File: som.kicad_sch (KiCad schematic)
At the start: 14 parts

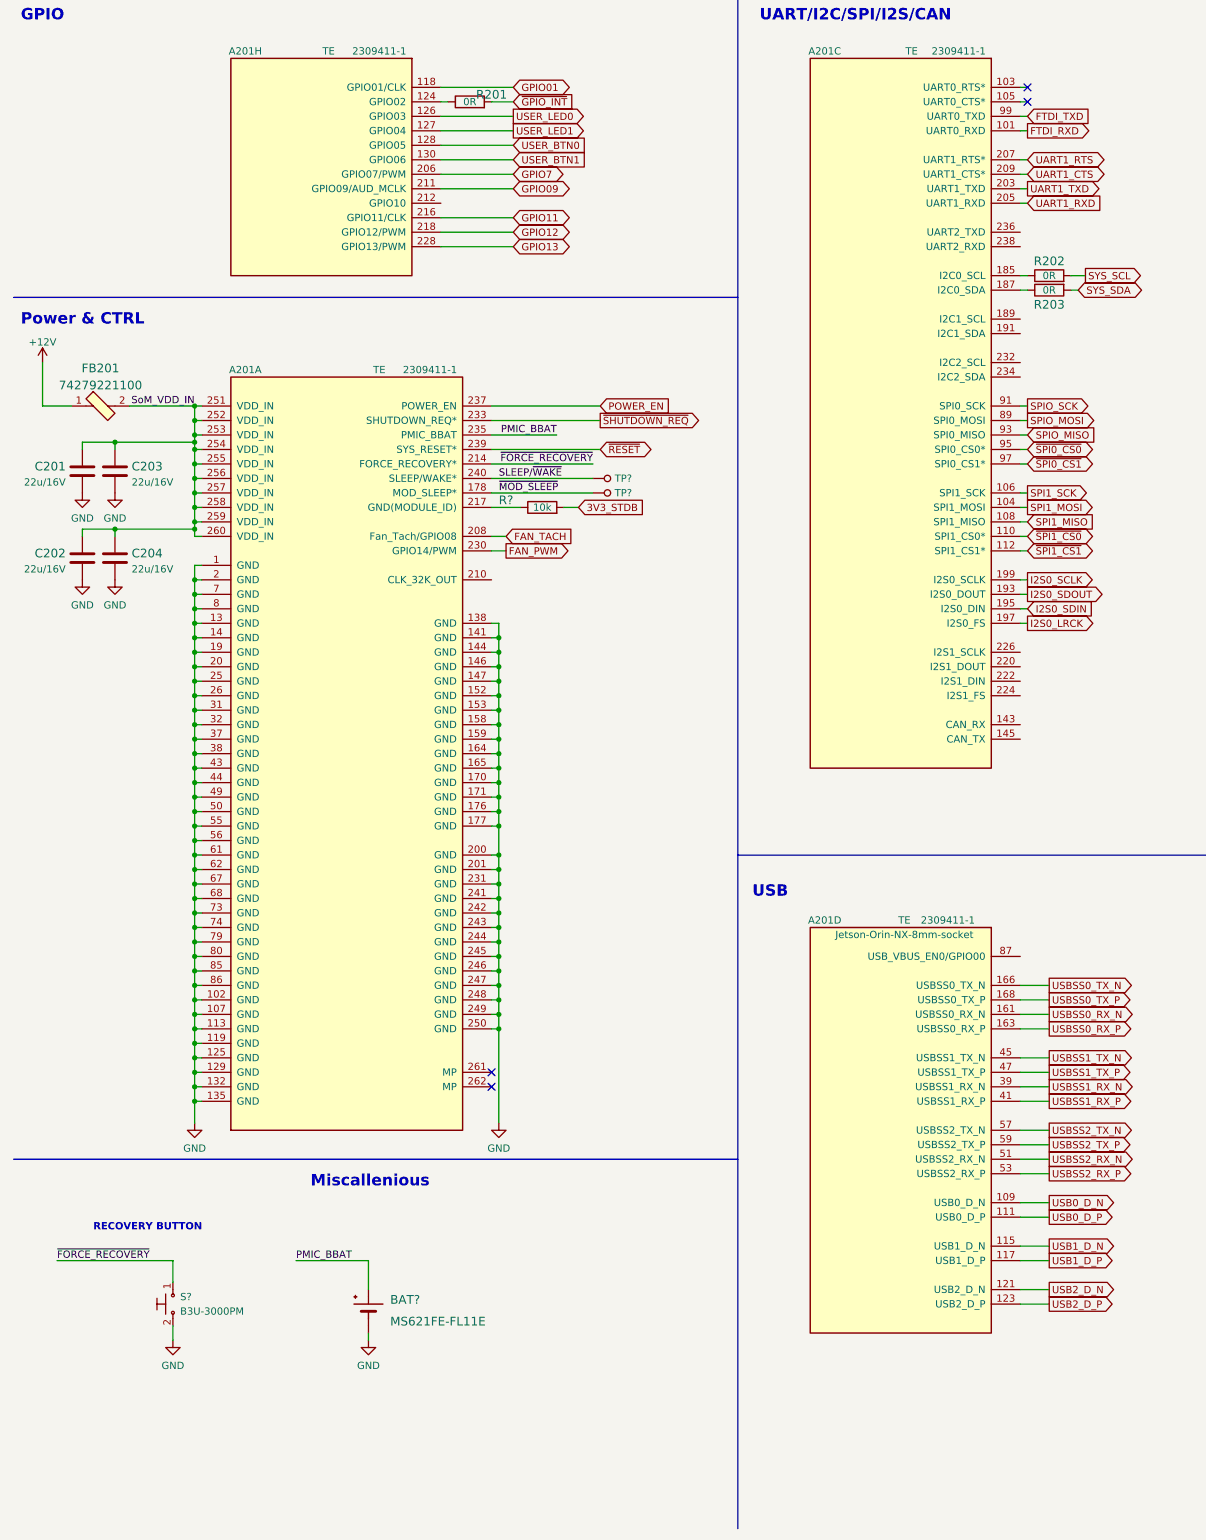
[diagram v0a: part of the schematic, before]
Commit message: Added buffer for debug UART
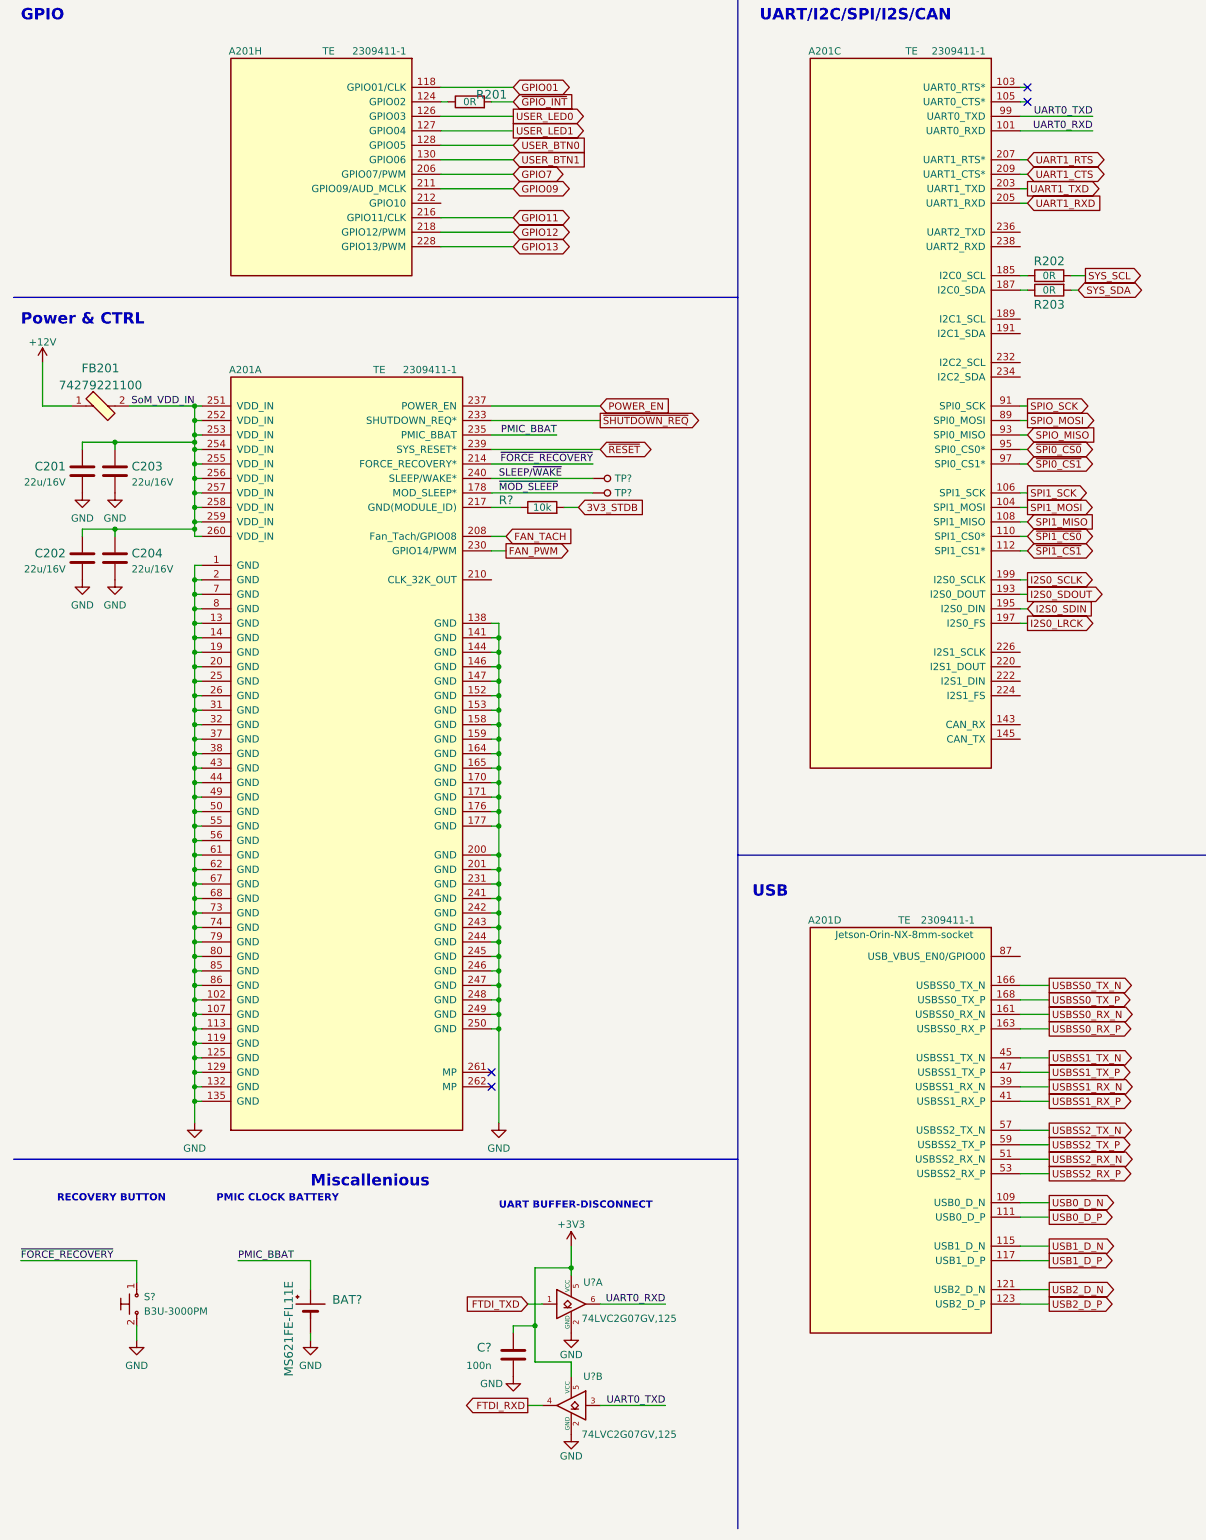
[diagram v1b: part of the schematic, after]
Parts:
- added C?: C_100n_0402, antmicro-footprints:0402-cap, symbol antmicroCapacitors0402:C_100n_0402
- added U? (x2): 74LVC2G07GV,125, antmicro-footprints:SC-74, symbol antmicroLogicBuffersDriversReceiversTransceivers:74LVC2G07GV,125
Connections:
- net FTDI_RXD: now also U?.4; no longer A201.101 (UART0_RXD)
- net FTDI_TXD: now also U?.1; no longer A201.99 (UART0_TXD)
- net GND: now also C?.2, U?.2 (GND), U?.2 (GND)
- new net +3V3: C?.1, U?.5 (VCC), U?.5 (VCC)
- new net UART0_RXD: A201.101 (UART0_RXD), U?.6
- new net UART0_TXD: A201.99 (UART0_TXD), U?.3
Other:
- note added: "PMIC CLOCK BATTERY"
- note added: "UART BUFFER-DISCONNECT"
- moved on the sheet: BAT?, S?

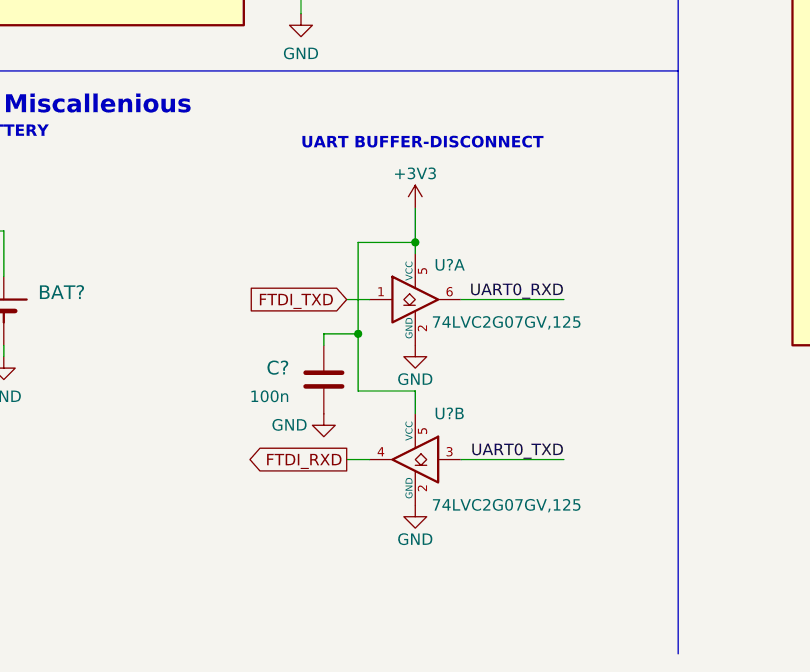
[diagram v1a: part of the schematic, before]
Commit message: Changed UART buffer for ones with push-pull output
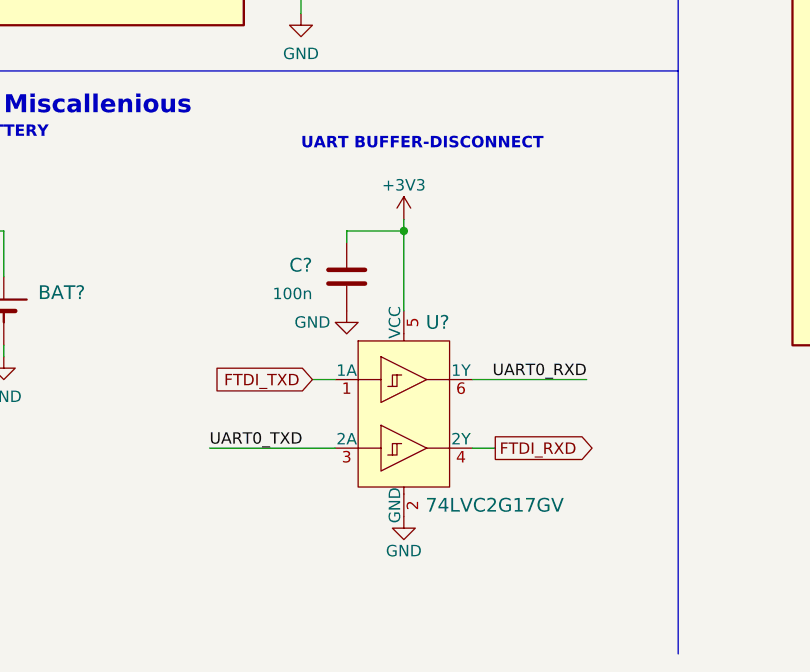
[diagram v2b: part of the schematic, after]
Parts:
- removed C?: C_100n_0402, antmicro-footprints:0402-cap, symbol antmicroCapacitors0402:C_100n_0402
- removed U? (x2): 74LVC2G07GV,125, antmicro-footprints:SC-74, symbol antmicroLogicBuffersDriversReceiversTransceivers:74LVC2G07GV,125
- added C?: C_100n_0402, antmicro-footprints:0402-cap, symbol antmicroCapacitors0402:C_100n_0402
- added U?: 74LVC2G17GV, antmicro-footprints:SC-74, symbol antmicroLogicBuffersDriversReceiversTransceivers:74LVC2G17GV
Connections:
- net +3V3: now also C?.1, U?.5 (VCC)
- net FTDI_RXD: now also U?.4 (2Y)
- net FTDI_TXD: now also U?.1 (1A)
- net GND: now also C?.2, U?.2 (GND)
- net UART0_RXD: now also U?.6 (1Y)
- net UART0_TXD: now also U?.3 (2A)

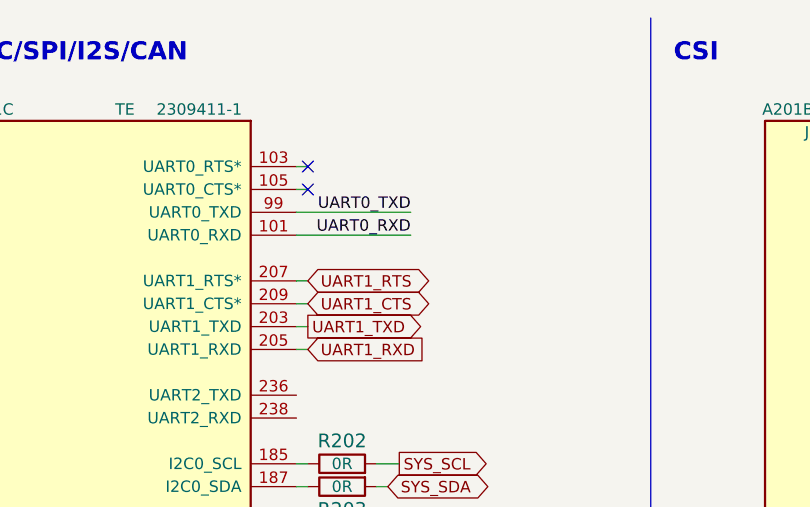
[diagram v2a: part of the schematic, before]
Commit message: Added 0Ohm resistors for debug UART
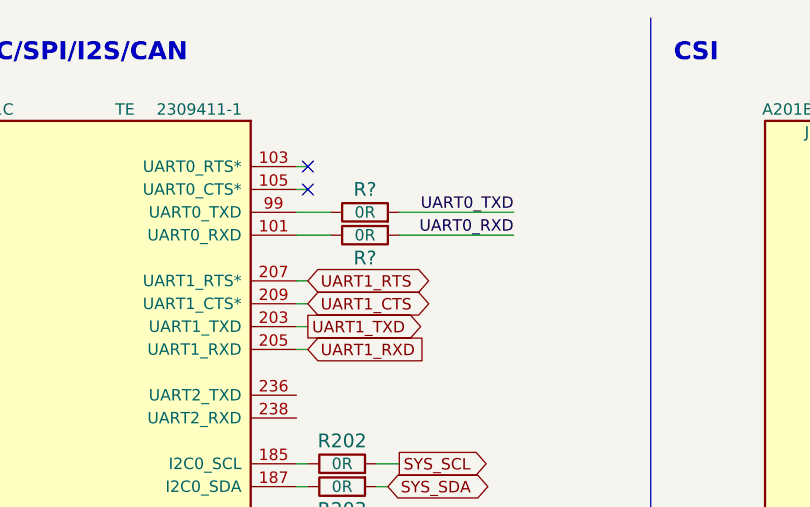
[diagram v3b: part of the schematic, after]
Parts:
- added R? (x2): R_0R_0402, antmicro-footprints:0402-res, symbol antmicroResistors0402:R_0R_0402
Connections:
- net UART0_RXD: now also R?.2; no longer A201.101 (UART0_RXD)
- net UART0_TXD: now also R?.2; no longer A201.99 (UART0_TXD)
- new net: A201.101 (UART0_RXD), R?.1
- new net: A201.99 (UART0_TXD), R?.1
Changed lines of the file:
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@@
     (stroke (width 0) (type default) (color 0 0 0 0))
   )
+  (wire (pts (xy 193.04 35.56) (xy 189.23 35.56))
+    (stroke (width 0) (type default) (color 0 0 0 0))
+  )
   (wire (pts (xy 119.38 260.35) (xy 116.84 260.35))
     (stroke (width 0) (type default) (color 0 0 0 0))
@@
     (stroke (width 0) (type default) (color 0 0 0 0))
   )
+  (wire (pts (xy 213.36 38.1) (xy 200.66 38.1))
+    (stroke (width 0) (type default) (color 0 0 0 0))
+  )
   (wire (pts (xy 200.66 63.5) (xy 198.12 63.5))
     (stroke (width 0) (type default) (color 0 0 0 0))
@@
     (stroke (width 0) (type default) (color 0 0 0 0))
   )
-  (wire (pts (xy 201.93 38.1) (xy 189.23 38.1))
-    (stroke (width 0) (type default) (color 0 0 0 0))
-  )
   (wire (pts (xy 279.4 55.88) (xy 278.13 55.88))
     (stroke (width 0) (type default) (color 0 0 0 0))
@@
     (stroke (width 0) (type default) (color 0 0 0 0))
   )
+  (wire (pts (xy 193.04 38.1) (xy 189.23 38.1))
+    (stroke (width 0) (type default) (color 0 0 0 0))
+  )
   (wire (pts (xy 97.79 139.7) (xy 97.79 137.16))
     (stroke (width 0) (type default) (color 0 0 0 0))
@@
     (stroke (width 0) (type default) (color 0 0 0 0))
   )
-  (wire (pts (xy 201.93 35.56) (xy 189.23 35.56))
-    (stroke (width 0) (type default) (color 0 0 0 0))
-  )
   (wire (pts (xy 115.57 86.36) (xy 96.52 86.36))
     (stroke (width 0) (type default) (color 0 0 0 0))
@@
     (stroke (width 0) (type default) (color 0 0 0 0))
   )
+  (wire (pts (xy 213.36 35.56) (xy 200.66 35.56))
+    (stroke (width 0) (type default) (color 0 0 0 0))
+  )
   (wire (pts (xy 34.29 247.65) (xy 34.29 250.19))
     (stroke (width 0) (type default) (color 0 0 0 0))
@@
     (effects (font (size 1.27 1.27)) (justify left bottom))
   )
-  (label "UART0_RXD" (at 201.93 38.1 180)
+  (label "UART0_RXD" (at 213.36 38.1 180)
     (effects (font (size 1.27 1.27)) (justify right bottom))
   )
@@
     (effects (font (size 1.27 1.27)) (justify left bottom))
   )
-  (label "UART0_TXD" (at 201.93 35.56 180)
+  (label "UART0_TXD" (at 213.36 35.56 180)
     (effects (font (size 1.27 1.27)) (justify right bottom))
   )
@@
     (pin "2")
   )
+  (symbol (lib_id "antmicroResistors0402:R_0R_0402") (at 196.85 35.56 0) (unit 1)
+    (in_bom yes) (on_board yes)
+    (property "Reference" "R?" (id 0) (at 196.85 33.02 0)
+      (effects (font (size 1.524 1.524)))
+    )
+    (property "Value" "R_0R_0402" (id 1) (at 196.85 39.37 0)
+      (effects (font (size 1.524 1.524)) hide)
+    )
+    (property "Footprint" "antmicro-footprints:0402-res" (id 2) (at 201.93 30.48 0)
+      (effects (font (size 1.524 1.524)) (justify left) hide)
+    )
+    (property "Datasheet" "" (id 3) (at 196.85 35.56 0)
+      (effects (font (size 1.27 1.27)) hide)
+    )
+    (property "Manufacturer" "PANASONIC" (id 4) (at 201.93 25.4 0)
+      (effects (font (size 1.524 1.524)) (justify left) hide)
+    )
+    (property "MPN" "ERJ2GE0R00X" (id 5) (at 201.93 27.94 0)
+      (effects (font (size 1.524 1.524)) (justify left) hide)
+    )
+    (property "Val" "0R" (id 6) (at 196.85 35.56 0))
+    (pin "1")
+    (pin "2")
+  )
   (symbol (lib_id "power:GND") (at 30.48 116.84 0) (unit 1)
     (in_bom yes) (on_board yes) (fields_autoplaced)
@@
     (pin "1")
   )
+  (symbol (lib_id "antmicroResistors0402:R_0R_0402") (at 196.85 38.1 0) (mirror x) (unit 1)
+    (in_bom yes) (on_board yes)
+    (property "Reference" "R?" (id 0) (at 196.85 40.64 0)
+      (effects (font (size 1.524 1.524)))
+    )
+    (property "Value" "R_0R_0402" (id 1) (at 196.85 34.29 0)
+      (effects (font (size 1.524 1.524)) hide)
+    )
+    (property "Footprint" "antmicro-footprints:0402-res" (id 2) (at 201.93 43.18 0)
+      (effects (font (size 1.524 1.524)) (justify left) hide)
+    )
+    (property "Datasheet" "" (id 3) (at 196.85 38.1 0)
+      (effects (font (size 1.27 1.27)) hide)
+    )
+    (property "Manufacturer" "PANASONIC" (id 4) (at 201.93 48.26 0)
+      (effects (font (size 1.524 1.524)) (justify left) hide)
+    )
+    (property "MPN" "ERJ2GE0R00X" (id 5) (at 201.93 45.72 0)
+      (effects (font (size 1.524 1.524)) (justify left) hide)
+    )
+    (property "Val" "0R" (id 6) (at 196.85 38.1 0))
+    (pin "1")
+    (pin "2")
+  )
   (symbol (lib_id "antmicroSoMConnectors:Jetson-Orin-NX-8mm-socket") (at 361.95 25.4 0) (mirror y) (unit 6)

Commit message: Readability improvements
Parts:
- added R207, R208: R_0R_0402, antmicro-footprints:0402-res, symbol antmicroResistors0402:R_0R_0402
- gave numbers to parts that had none: 9
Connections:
- net at A201.189 (I2C1_SCL): now also R207.1
- net at A201.191 (I2C1_SDA): now also R208.1
- new net I2C1_SCL: R207.2
- new net I2C1_SDA: R208.2
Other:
- note removed: "To "M.2" Sub-schematic"
- moved on the sheet: R202, R203

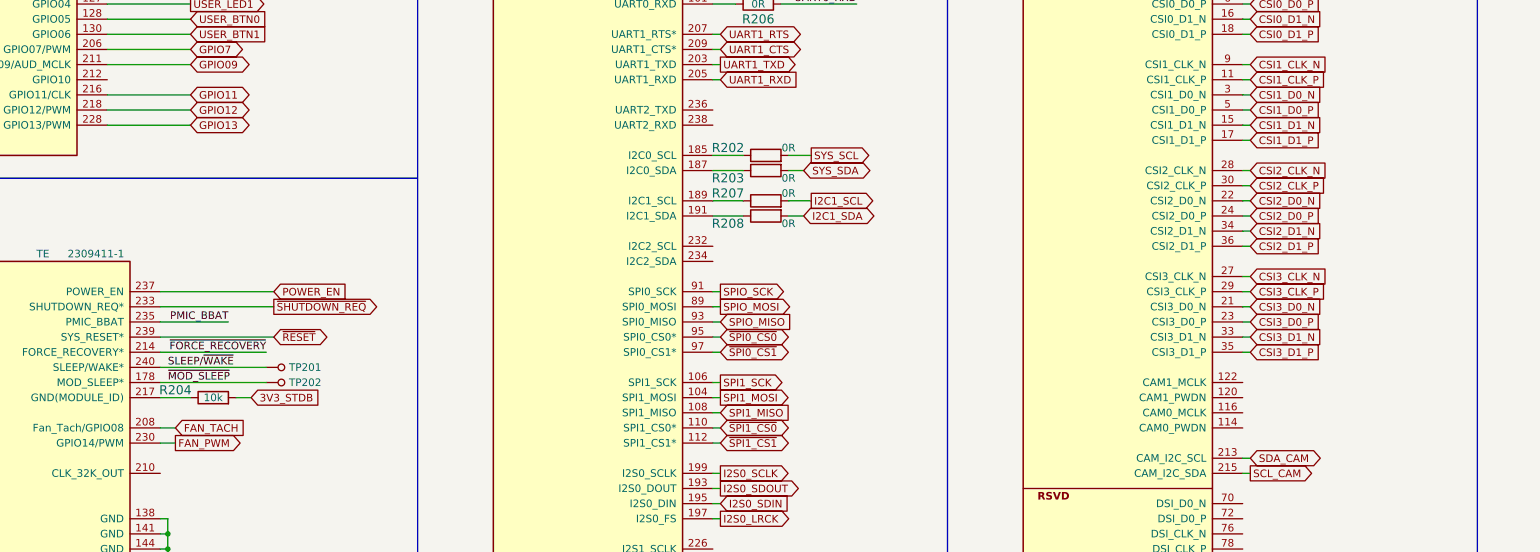
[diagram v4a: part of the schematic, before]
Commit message: Connected VSYNC signals
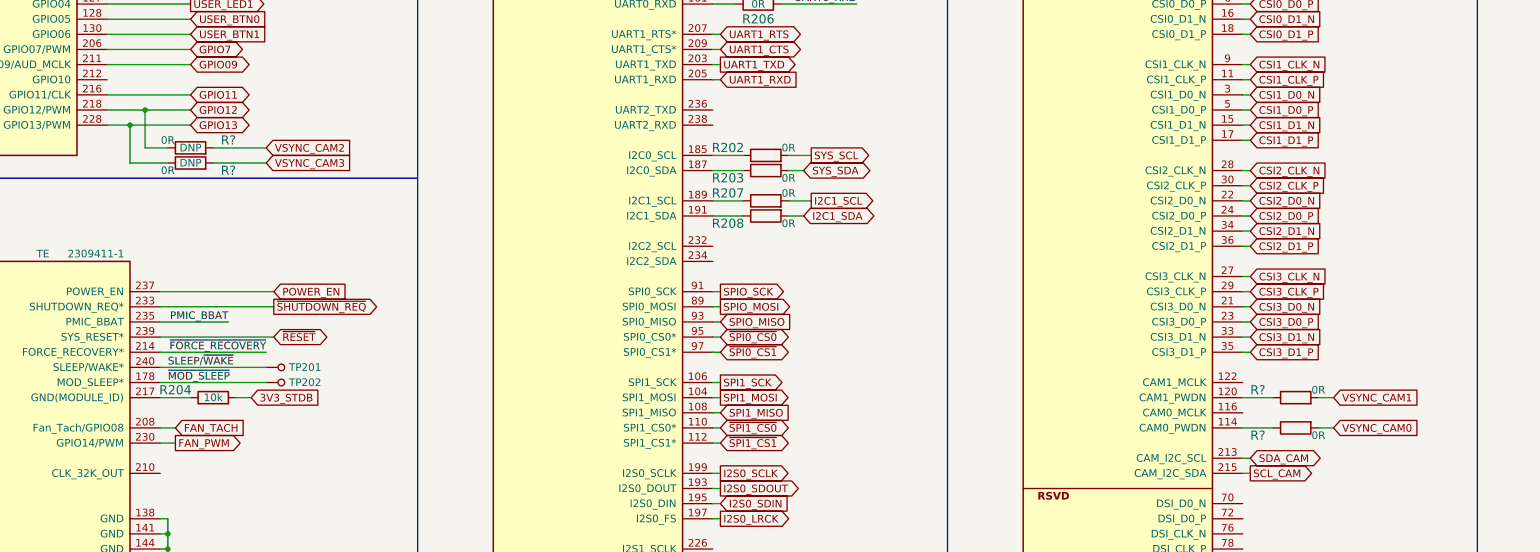
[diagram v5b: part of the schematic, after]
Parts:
- added R? (x4): R_0R_0402, antmicro-footprints:0402-res, symbol antmicroResistors0402:R_0R_0402
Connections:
- net GPIO12: now also R?.1
- net GPIO13: now also R?.1
- net at A201.114 (CAM0_PWDN): now also R?.1
- net at A201.120 (CAM1_PWDN): now also R?.1
- new net VSYNC_CAM0: R?.2
- new net VSYNC_CAM1: R?.2
- new net VSYNC_CAM2: R?.2
- new net VSYNC_CAM3: R?.2
